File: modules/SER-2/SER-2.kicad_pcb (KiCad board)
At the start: 2 copper layers, 160 x 100 mm, 19 parts, among them J1 CardConnector, J2 CPU GRANT CONFIGURATION, U1 74AHCT541, U2 74AHCT541, U3 74AHCT245, U4 74AHCT541, U5 74AHCT541, U6 74HCT10, U7 W65C02, Y1 1Mhz

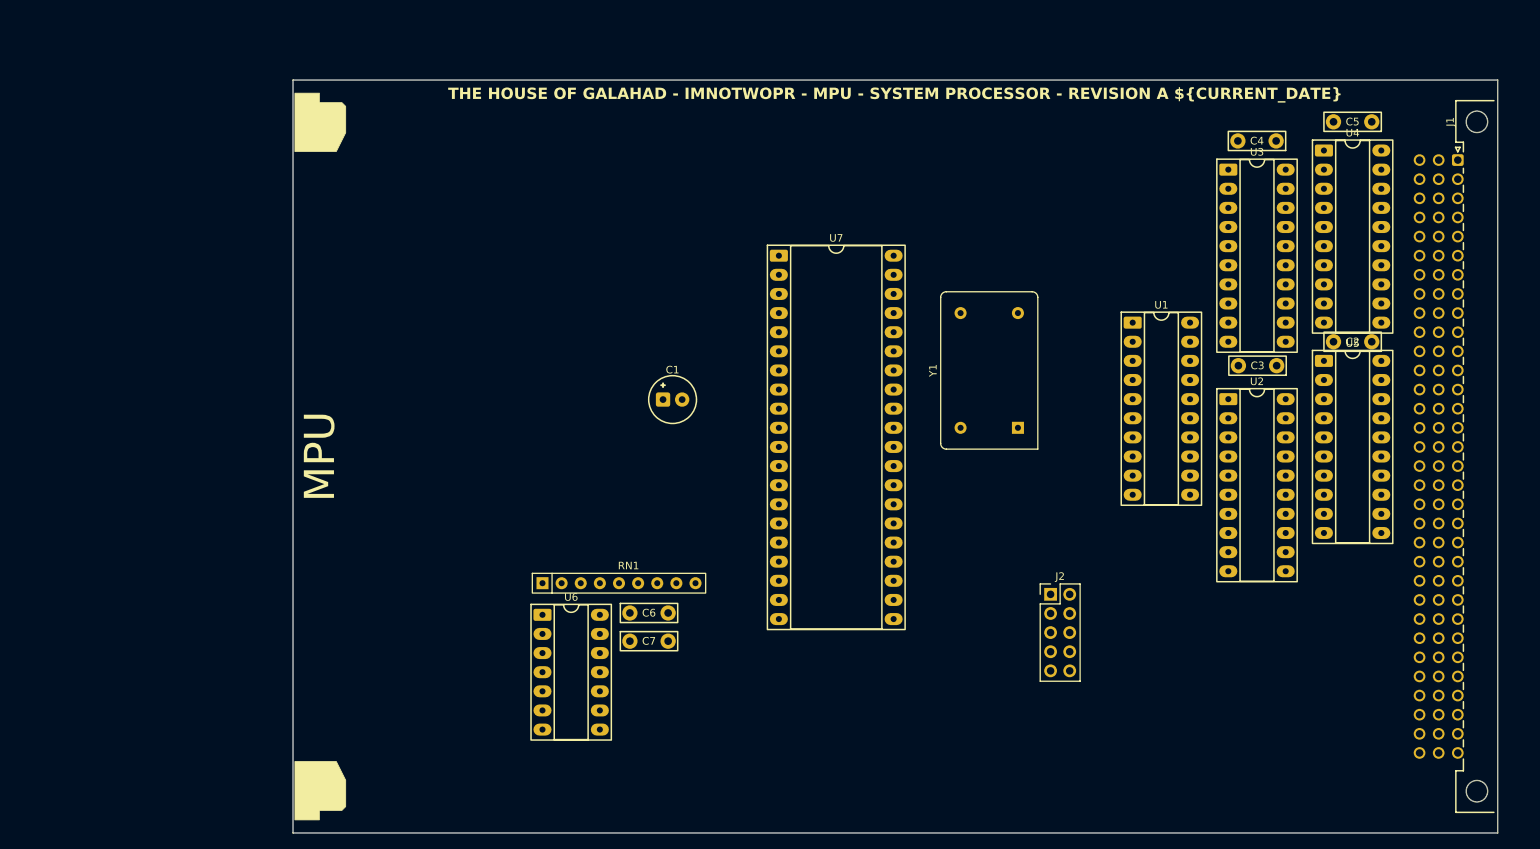
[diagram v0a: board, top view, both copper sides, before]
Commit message: migrated PWR to SCC; updates to MPU, more work pending
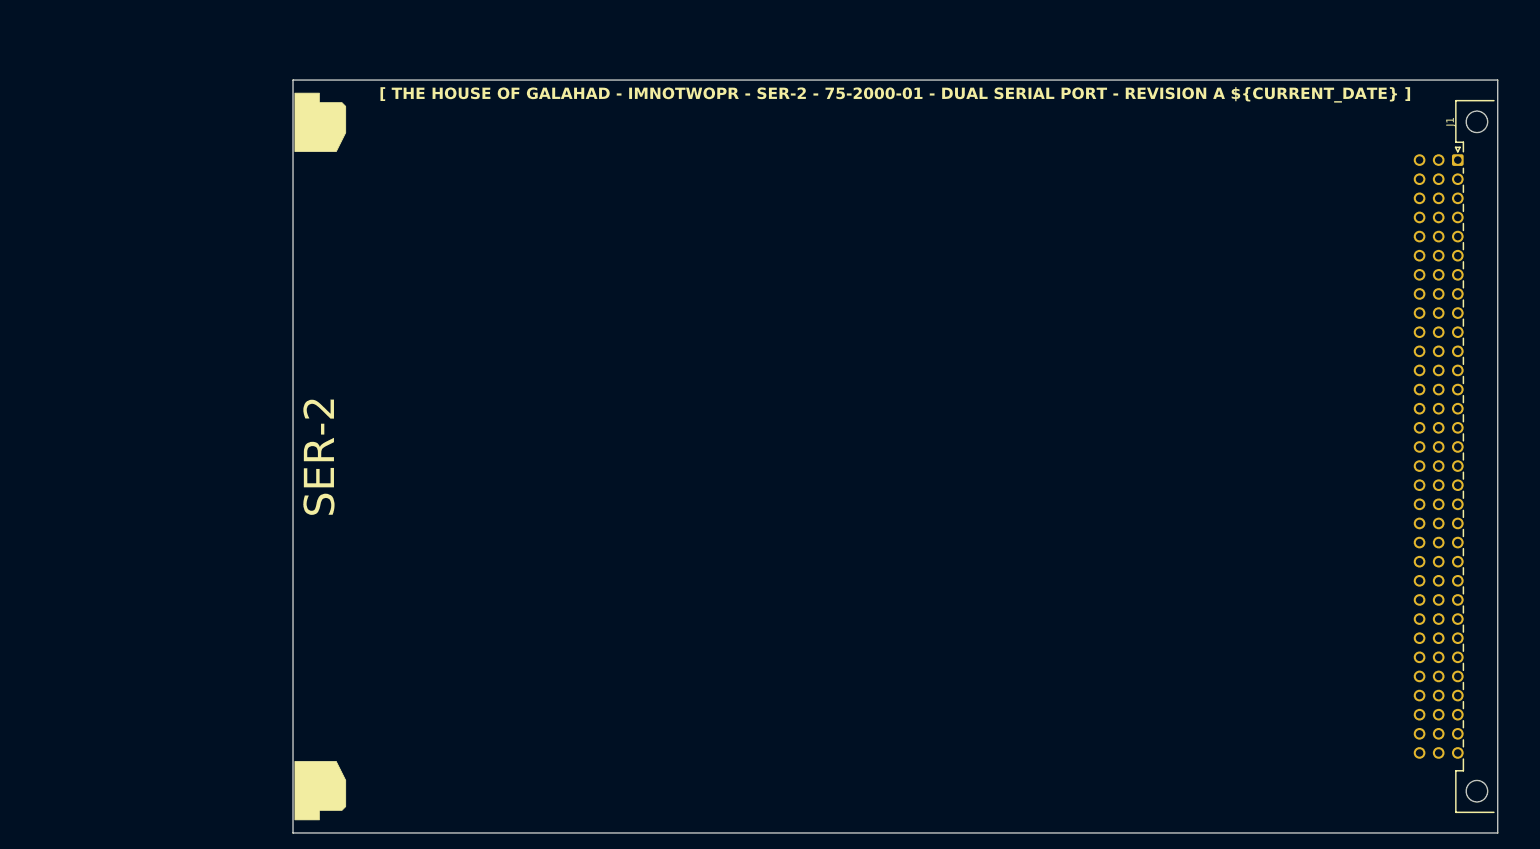
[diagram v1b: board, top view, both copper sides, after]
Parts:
- removed C1: 47u, IMNOTWOPR:CP_Radial_Tantal_P100mil
- removed C2, C3, C4, C5, C6, C7: 100n, FormantKO:C_Rect_P200mil
- removed J2: CPU GRANT CONFIGURATION, Connector_PinHeader_2.54mm:PinHeader_2x05_P2.54mm_Vertical
- removed RN1: 10k, Resistor_THT:R_Array_SIP9
- removed U1, U2, U4, U5: 74AHCT541, IMNOTWOPR:DIP-20N
- removed U3: 74AHCT245, IMNOTWOPR:DIP-20N
- removed U6: 74HCT10, IMNOTWOPR:DIP-14N
- removed U7: W65C02, IMNOTWOPR:DIP-40W
- removed Y1: 1Mhz, Oscillator:Oscillator_DIP-14
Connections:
- J1 pad a10: /SA6 -> /TEMPLATE/S6
- J1 pad a11: /SA7 -> /TEMPLATE/S7
- J1 pad a12: /SA8 -> /TEMPLATE/S8
- J1 pad a13: /SA9 -> /TEMPLATE/S9
- J1 pad a14: /SA10 -> /TEMPLATE/S10
- J1 pad a15: /SA11 -> /TEMPLATE/S11
- J1 pad a16: /SA12 -> /TEMPLATE/S12
- J1 pad a17: /SA13 -> /TEMPLATE/S13
- J1 pad a18: /SA14 -> /TEMPLATE/S14
- J1 pad a19: /SA15 -> /TEMPLATE/S15
- J1 pad a4: /SA0 -> /TEMPLATE/S0
- J1 pad a5: /SA1 -> /TEMPLATE/S1
- J1 pad a6: /SA2 -> /TEMPLATE/S2
- J1 pad a7: /SA3 -> /TEMPLATE/S3
- J1 pad a8: /SA4 -> /TEMPLATE/S4
- J1 pad a9: /SA5 -> /TEMPLATE/S5
- J1 pad b10: Net-(J1B-READY) -> unconnected-(J1B-D_{6}-Padb10)
- J1 pad b11: Net-(J1B-BE) -> unconnected-(J1B-D_{7}-Padb11)
- J1 pad b12: Net-(J1B-SYNC) -> unconnected-(J1B-Φ_{2}-Padb12)
- J1 pad b13: Net-(J1B-VPB) -> unconnected-(J1B-R~{W}-Padb13)
- J1 pad b14: Net-(J1B-MLB) -> unconnected-(J1B-VALID-Padb14)
- J1 pad b22: /SD0 -> unconnected-(J1B-~{BUS_ACK}-Padb22)
- J1 pad b23: /SD1 -> unconnected-(J1B-~{ABORT}-Padb23)
- J1 pad b24: /SD2 -> unconnected-(J1B-SYNC-Padb24)
- J1 pad b25: /SD3 -> unconnected-(J1B-VPB-Padb25)
- J1 pad b26: /SD4 -> unconnected-(J1B-MLB-Padb26)
- J1 pad b27: /SD5 -> unconnected-(J1B-VDA-Padb27)
- J1 pad b28: /SD6 -> unconnected-(J1B-VPA-Padb28)
- J1 pad b29: /SD7 -> unconnected-(J1B-RESERVED-Padb29)
- J1 pad b4: Net-(J1B-/VALID) -> unconnected-(J1B-D_{0}-Padb4)
- J1 pad b5: Net-(J1B-PHI2) -> unconnected-(J1B-D_{1}-Padb5)
- J1 pad b6: Net-(J1B-R/W) -> unconnected-(J1B-D_{2}-Padb6)
- J1 pad b7: Net-(J1B-/RESET) -> unconnected-(J1B-D_{3}-Padb7)
- J1 pad b8: Net-(J1B-/IRQ) -> unconnected-(J1B-D_{4}-Padb8)
- J1 pad b9: Net-(J1B-/NMI) -> unconnected-(J1B-D_{5}-Padb9)
- J1 pad c21: Net-(J1C-/BUSGNT0) -> unconnected-(J1C-RESERVED-Padc21)
- J1 pad c23: Net-(J1C-/BUSGNT1) -> unconnected-(J1C-RESERVED-Padc23)
- J1 pad c26: Net-(J1C-/BUSGNT2) -> unconnected-(J1C-MX-Padc26)
- J1 pad c28: Net-(J1C-/BUSGNT3) -> unconnected-(J1C-RESERVED-Padc28)
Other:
- board text added: "[ ${COMPANY} - ${COMMENT1} - ${TITLE} - ${COMMENT4} - ${COMMENT2} - REVISION ${REVISION} ${CURRENT_DATE} ]"
- board text removed: "${COMPANY} - ${COMMENT1} - ${TITLE} - ${COMMENT2} - REVISION ${REVISION} ${CURRENT_DATE}"

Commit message: work on ser-2 board. library cleanup
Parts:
- added C1: 47u, IMNOTWOPR:CP_Radial_Tantal_P100mil, F.Cu at (175.4, 122.8)
- added C10: 100n, IMNOTWOPR:C_Rect_P200mil, F.Cu at (195.7, 98.8)
- added C11: 100n, IMNOTWOPR:C_Rect_P200mil, F.Cu at (128.4, 95.0)
- added C12: 100n, IMNOTWOPR:C_Rect_P200mil, F.Cu at (97.9, 95.0)
- added C13: 100n, IMNOTWOPR:C_Rect_P200mil, F.Cu at (125.9, 70.9)
- added C14: 100n, IMNOTWOPR:C_Rect_P200mil, F.Cu at (91.6, 70.9)
- added C15: 100n, IMNOTWOPR:C_Rect_P200mil, F.Cu at (181.1, 39.3)
- added C16: 100n, IMNOTWOPR:C_Rect_P200mil, F.Cu at (181.1, 42.6)
- added C17: 100n, IMNOTWOPR:C_Rect_P200mil, F.Cu at (193.2, 135.6)
- added C18: 100n, IMNOTWOPR:C_Rect_P200mil, F.Cu at (183.0, 139.4)
- added C19: 20pf, IMNOTWOPR:C_Rect_P200mil, F.Cu at (148.7, 129.3)
- added C2: 47u, IMNOTWOPR:CP_Radial_Tantal_P100mil, F.Cu at (175.4, 131.4)
- added C20: 20pf, IMNOTWOPR:C_Rect_P200mil, F.Cu at (118.3, 129.3)
- added C3: 47u, IMNOTWOPR:CP_Radial_Tantal_P100mil, F.Cu at (198.3, 46.7)
- added C4: 100n, IMNOTWOPR:C_Rect_P200mil, F.Cu at (23.0, 72.7)
- added C5: 100n, IMNOTWOPR:C_Rect_P200mil, F.Cu at (23.0, 76.0)
- added C6: 100n, IMNOTWOPR:C_Rect_P200mil, F.Cu at (195.7, 55.6)
- added C7: 100n, IMNOTWOPR:C_Rect_P200mil, F.Cu at (21.7, 81.6)
- added C8: 100n, IMNOTWOPR:C_Rect_P200mil, F.Cu at (21.7, 84.8)
- added C9: 100n, IMNOTWOPR:C_Rect_P200mil, F.Cu at (183.0, 76.0)
- added D1: LED_G, IMNOTWOPR:LED_D5.0mm_Horizontal_O1.27mm_Z3.0mm, F.Cu at (51.0, 77.2)
- added D10: LED_R, IMNOTWOPR:LED_D5.0mm_Horizontal_O1.27mm_Z3.0mm, F.Cu at (51.0, 98.8)
- added D11: LED_R, IMNOTWOPR:LED_D5.0mm_Horizontal_O3.81mm_Z9.0mm, F.Cu at (51.0, 98.8)
- added D12: LED_R, IMNOTWOPR:LED_D5.0mm_Horizontal_O3.81mm_Z9.0mm, F.Cu at (51.0, 111.5)
- added D13: LED_G, IMNOTWOPR:LED_D5.0mm_Horizontal_O1.27mm_Z3.0mm, F.Cu at (51.0, 111.5)
- added D14: LED_R, IMNOTWOPR:LED_D5.0mm_Horizontal_O1.27mm_Z3.0mm, F.Cu at (51.0, 105.2)
- added D15: LED_R, IMNOTWOPR:LED_D5.0mm_Horizontal_O3.81mm_Z9.0mm, F.Cu at (51.0, 77.2)
- added D16: LED_R, IMNOTWOPR:LED_D5.0mm_Horizontal_O3.81mm_Z9.0mm, F.Cu at (51.0, 117.9)
- added D17: 1N4148, FormantKO:DO-35_P400mil, F.Cu at (66.2, 82.3)
- added D18: 1N4148, FormantKO:DO-35_P400mil, F.Cu at (66.2, 122.9)
- added D2: LED_G, IMNOTWOPR:LED_D5.0mm_Horizontal_O3.81mm_Z9.0mm, F.Cu at (51.0, 64.5)
- added D3: LED_R, IMNOTWOPR:LED_D5.0mm_Horizontal_O1.27mm_Z3.0mm, F.Cu at (51.0, 58.2)
- added D4: LED_R, IMNOTWOPR:LED_D5.0mm_Horizontal_O3.81mm_Z9.0mm, F.Cu at (51.0, 58.2)
- added D5: LED_R, IMNOTWOPR:LED_D5.0mm_Horizontal_O3.81mm_Z9.0mm, F.Cu at (51.0, 70.9)
- added D6: LED_G, IMNOTWOPR:LED_D5.0mm_Horizontal_O1.27mm_Z3.0mm, F.Cu at (51.0, 70.9)
- added D7: LED_R, IMNOTWOPR:LED_D5.0mm_Horizontal_O1.27mm_Z3.0mm, F.Cu at (51.0, 64.5)
- added D8: LED_G, IMNOTWOPR:LED_D5.0mm_Horizontal_O1.27mm_Z3.0mm, F.Cu at (51.0, 117.9)
- added D9: LED_G, IMNOTWOPR:LED_D5.0mm_Horizontal_O3.81mm_Z9.0mm, F.Cu at (51.0, 105.2)
- added J2: DE-9 DTE, IMNOTWOPR:DE-9_IDC_2x05, F.Cu at (138.6, 56.9)
- added J3: DE-9 DTE, IMNOTWOPR:DE-9_IDC_2x05, F.Cu at (108.6, 56.9)
- added R1: 430R, IMNOTWOPR:R_Axial_DIN0207_P400mil, F.Cu at (72.5, 73.4)
- added R10: 430R, IMNOTWOPR:R_Axial_DIN0207_P400mil, F.Cu at (78.9, 103.9)
- added R11: 430R, IMNOTWOPR:R_Axial_DIN0207_P400mil, F.Cu at (72.5, 93.7)
- added R12: 430R, IMNOTWOPR:R_Axial_DIN0207_P400mil, F.Cu at (78.9, 97.5)
- added R13: 430R, IMNOTWOPR:R_Axial_DIN0207_P400mil, F.Cu at (78.9, 110.2)
- added R14: 430R, IMNOTWOPR:R_Axial_DIN0207_P400mil, F.Cu at (72.5, 107.7)
- added R15: 430R, IMNOTWOPR:R_Axial_DIN0207_P400mil, F.Cu at (72.5, 101.3)
- added R16: 1M, IMNOTWOPR:R_Axial_DIN0207_P400mil, F.Cu at (101.8, 139.4)
- added R17: 680R, IMNOTWOPR:R_Axial_DIN0207_P400mil, F.Cu at (78.9, 76.1)
- added R18: 680R, IMNOTWOPR:R_Axial_DIN0207_P400mil, F.Cu at (78.9, 116.6)
- added R2: 430R, IMNOTWOPR:R_Axial_DIN0207_P400mil, F.Cu at (78.9, 63.2)
- added R3: 430R, IMNOTWOPR:R_Axial_DIN0207_P400mil, F.Cu at (72.5, 54.4)
- added R4: 430R, IMNOTWOPR:R_Axial_DIN0207_P400mil, F.Cu at (78.9, 56.9)
- added R5: 430R, IMNOTWOPR:R_Axial_DIN0207_P400mil, F.Cu at (78.9, 69.6)
- added R6: 430R, IMNOTWOPR:R_Axial_DIN0207_P400mil, F.Cu at (72.5, 67.1)
- added R7: 430R, IMNOTWOPR:R_Axial_DIN0207_P400mil, F.Cu at (72.5, 60.7)
- added R8: 1M, IMNOTWOPR:R_Axial_DIN0207_P400mil, F.Cu at (119.8, 139.4)
- added R9: 430R, IMNOTWOPR:R_Axial_DIN0207_P400mil, F.Cu at (72.5, 114.0)
- added RN1: 10kΩ, Resistor_THT:R_Array_SIP9, F.Cu at (152.6, 55.6)
- added SW1: PAGE SELECT, Button_Switch_THT:SW_DIP_SPSTx08_Slide_9.78x22.5mm_W7.62mm_P2.54mm, F.Cu at (155.1, 67.1)
- added U1: MC1488, FormantKO:DIP-14N, F.Cu at (133.5, 84.8)
- added U10: 74HCT688, IMNOTWOPR:DIP-20N, F.Cu at (164.0, 76.0)
- added U11: MC1489, FormantKO:DIP-14N, F.Cu at (133.5, 72.1)
- added U12: MC1489, FormantKO:DIP-14N, F.Cu at (103.0, 72.1)
- added U13: 74HCT138, IMNOTWOPR:DIP-16N, F.Cu at (158.9, 88.7)
- added U2: 74AHCT541, IMNOTWOPR:DIP-20N, F.Cu at (195.7, 72.1)
- added U3: MC1488, FormantKO:DIP-14N, F.Cu at (103.0, 84.8)
- added U4: 74AHCT541, IMNOTWOPR:DIP-20N, F.Cu at (184.3, 92.5)
- added U5: 74HCT00, IMNOTWOPR:DIP-14N, F.Cu at (157.6, 102.6)
- added U6: 74HCT32, IMNOTWOPR:DIP-14N, F.Cu at (172.9, 106.4)
- added U7: 74AHCT245, IMNOTWOPR:DIP-20N, F.Cu at (195.7, 115.3)
- added U8: W65C51, IMNOTWOPR:DIP-28W, F.Cu at (133.5, 115.3)
- added U9: W65C51, IMNOTWOPR:DIP-28W, F.Cu at (103.0, 115.3)
- added Y1: 1.8432Mhz, Crystal:Crystal_HC49-U_Vertical, F.Cu at (148.7, 121.6)
- added Y2: 1.8432Mhz, Crystal:Crystal_HC49-U_Vertical, F.Cu at (118.3, 121.5)
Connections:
- J1 pad a10: /TEMPLATE/S6 -> /SER-2/SA6
- J1 pad a11: /TEMPLATE/S7 -> /SER-2/SA7
- J1 pad a12: /TEMPLATE/S8 -> /SER-2/SA8
- J1 pad a13: /TEMPLATE/S9 -> /SER-2/SA9
- J1 pad a14: /TEMPLATE/S10 -> /SER-2/SA10
- J1 pad a15: /TEMPLATE/S11 -> /SER-2/SA11
- J1 pad a16: /TEMPLATE/S12 -> /SER-2/SA12
- J1 pad a17: /TEMPLATE/S13 -> /SER-2/SA13
- J1 pad a18: /TEMPLATE/S14 -> /SER-2/SA14
- J1 pad a19: /TEMPLATE/S15 -> /SER-2/SA15
- J1 pad a3: unconnected-(J1A-+12V-Pada3) -> +12V
- J1 pad a30: unconnected-(J1A-+12V-Pada30) -> +12V
- J1 pad a4: /TEMPLATE/S0 -> /SER-2/SA0
- J1 pad a5: /TEMPLATE/S1 -> /SER-2/SA1
- J1 pad a6: /TEMPLATE/S2 -> /SER-2/SA2
- J1 pad a7: /TEMPLATE/S3 -> /SER-2/SA3
- J1 pad a8: /TEMPLATE/S4 -> /SER-2/SA4
- J1 pad a9: /TEMPLATE/S5 -> /SER-2/SA5
- J1 pad b22: unconnected-(J1B-~{BUS_ACK}-Padb22) -> /SER-2/SD0
- J1 pad b23: unconnected-(J1B-~{ABORT}-Padb23) -> /SER-2/SD1
- J1 pad b24: unconnected-(J1B-SYNC-Padb24) -> /SER-2/SD2
- J1 pad b25: unconnected-(J1B-VPB-Padb25) -> /SER-2/SD3
- J1 pad b26: unconnected-(J1B-MLB-Padb26) -> /SER-2/SD4
- J1 pad b27: unconnected-(J1B-VDA-Padb27) -> /SER-2/SD5
- J1 pad b28: unconnected-(J1B-VPA-Padb28) -> /SER-2/SD6
- J1 pad b29: unconnected-(J1B-RESERVED-Padb29) -> /SER-2/SD7
- J1 pad b3: unconnected-(J1B--12V-Padb3) -> -12V
- J1 pad b30: unconnected-(J1B--12V-Padb30) -> -12V
- J1 pad b4: unconnected-(J1B-D_{0}-Padb4) -> /SER-2/~{VALID}
- J1 pad b5: unconnected-(J1B-D_{1}-Padb5) -> /SER-2/PHI2
- J1 pad b6: unconnected-(J1B-D_{2}-Padb6) -> /SER-2/R/W
- J1 pad b7: unconnected-(J1B-D_{3}-Padb7) -> /SER-2/~{RESET}
- J1 pad b8: unconnected-(J1B-D_{4}-Padb8) -> /SER-2/~{IRQ}
